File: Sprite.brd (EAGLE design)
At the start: 35 x 35 mm, 28 parts, among them P1 SPRITE_PIN, P2 SPRITE_PIN, U1 CC430F5137, U2 LSM9DS1, X1 TCXO_7Z

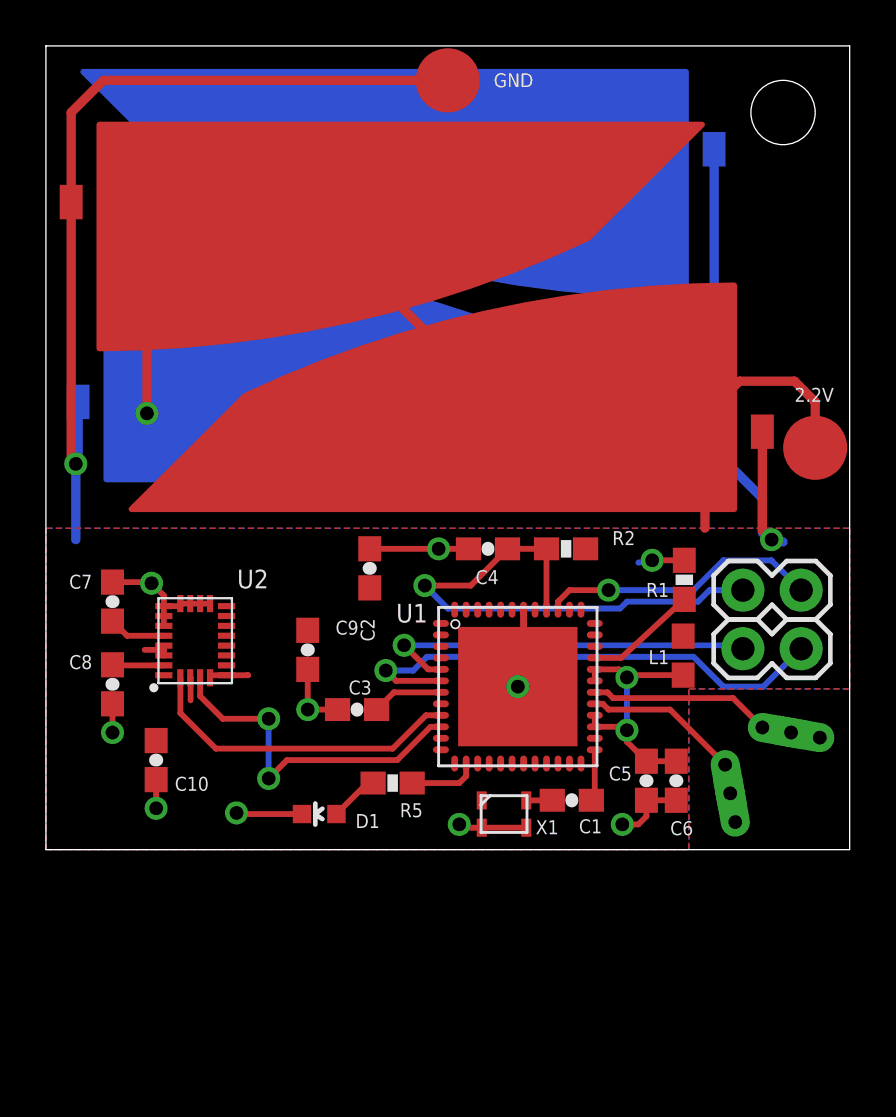
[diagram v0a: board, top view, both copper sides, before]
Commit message: New outline with board spring
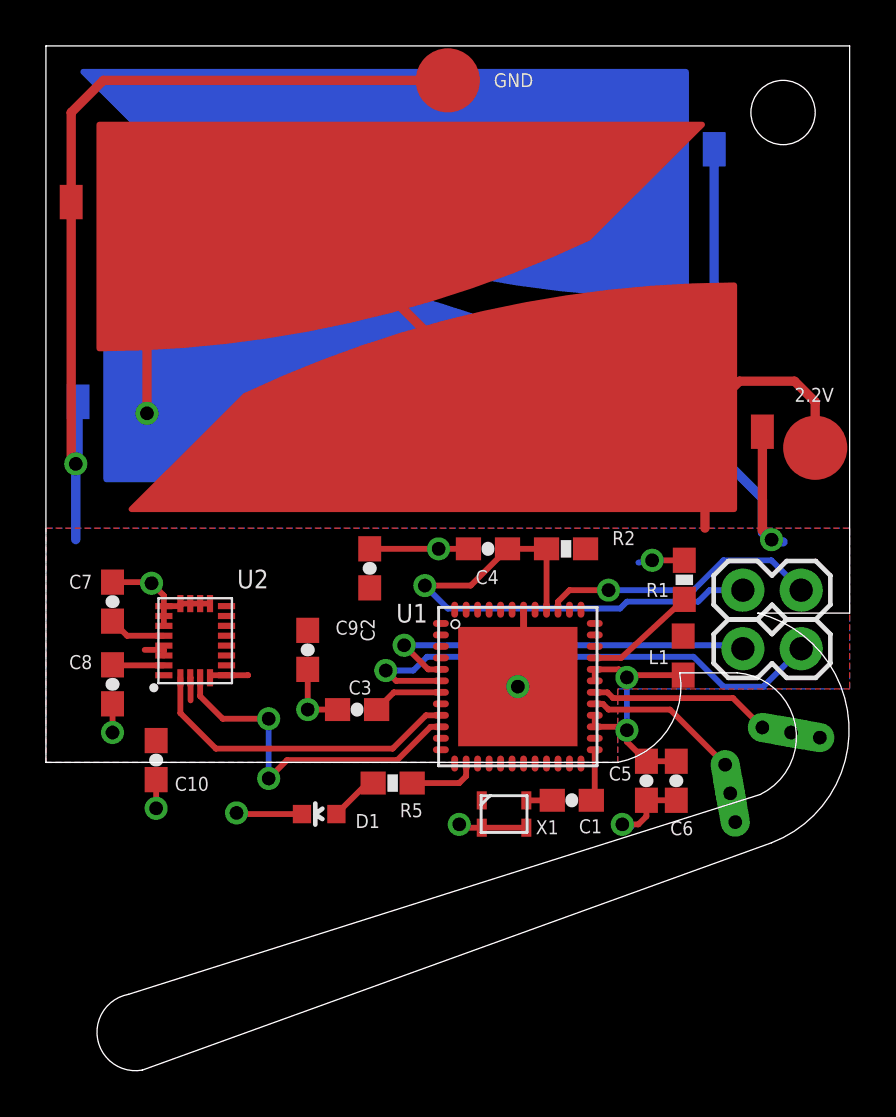
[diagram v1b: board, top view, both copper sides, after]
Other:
- board size 35 x 35 mm -> 35 x 44.6 mm

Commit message: moved solar cells + antenna on new board
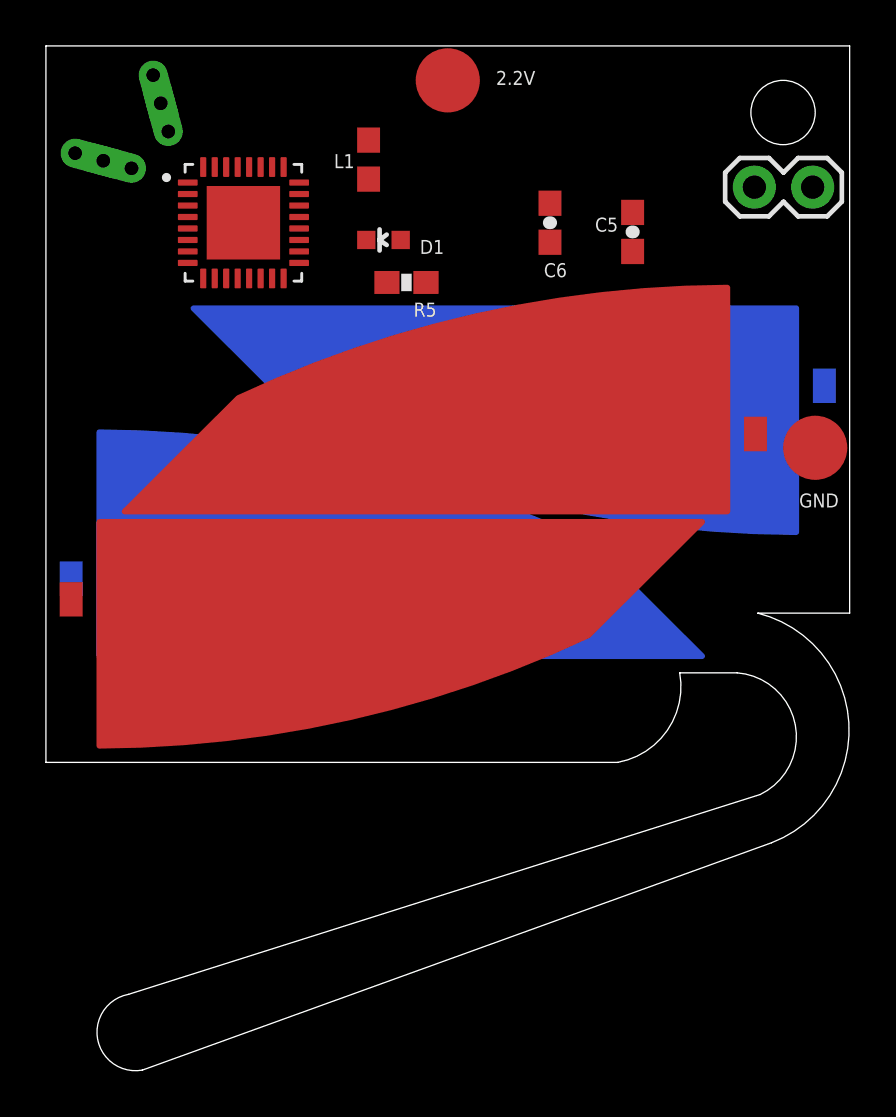
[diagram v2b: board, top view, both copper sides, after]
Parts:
- removed C1: 10 nF, SparkFun:0603-CAP
- removed C10: 10uF, SparkFun:0603-CAP
- removed C2, C3: 470nF, SparkFun:0603-CAP
- removed C4: 2.2nF, SparkFun:0603-CAP
- removed C7: 10nF, SparkFun:0603-CAP
- removed C8, C9: 0.1uF, SparkFun:0603-CAP
- removed JP2: (no value), SparkFun:1X02
- removed R1: 56K, SparkFun:0603-RES
- removed R2: 47K, SparkFun:0603-RES
- removed U2: LSM9DS1, LSM9DS1:LGA24-8X4
- removed X1: TCXO_7Z, SpriteTCXO:TXC_7Z
- U1: value CC430F5137 -> CC1310F128RHB; device TI_MSP430_v16:RGZ48 -> CC1310F128RHB:QFN50P500X500X100-33N
- moved ANT-P 39.0 mm to (5.00, 32.5), turned to 105 degrees
- moved ANT-N 38.9 mm to (2.50, 30.0), turned to 345 degrees
- moved S4 36.4 mm to (2.20, 8.30), turned to 0 degrees
- moved S2 32.5 mm to (29.8, 14.6), turned to 0 degrees
- moved S3 31.3 mm to (32.8, 23.7), turned to 180 degrees
- moved S1 27.9 mm to (2.20, 14.4), turned to 180 degrees
- moved L1 25.6 mm to (14.1, 30.1)
- moved D1 25.2 mm to (14.7, 26.6)
- moved C6 24.9 mm to (21.9, 27.3)
- moved C5 23.9 mm to (25.6, 26.9)
- moved U1 23.5 mm to (8.60, 27.3)
- moved R5 21.8 mm to (15.7, 24.7)
- moved JP3 20.1 mm to (30.9, 28.9)
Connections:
- removed net N$1: C1.1, U1.25
- removed net N$12: C1.2, X1.OUT
- removed net N$3: R1.1, U1.33
- removed net N$4: C3.1, U1.7
- removed net N$5: C7.1, U2.21
- removed net N$6: C8.1, U2.24
- removed net RST: C4.2, JP2.1, R2.1, U1.40
- removed net SCL: U1.9, U2.2
- removed net SDA: U1.10, U2.4
- removed net TEST: JP2.2, U1.39
- new net VDDR: U1.29
- new net VDDR_RF: U1.32
- new net VDDS: U1.28
- new net VDDSZ: U1.11
- new net VDDS_DCDC: U1.18
- net GND: now also P2.PIN; no longer C10.2, C2.2, C3.2, C4.1, C7.2, C8.2, C9.2, P1.PIN, R1.2, U1.42, U1.TP, U2.14, U2.15, U2.16, U2.17, U2.18, U2.19, U2.20, X1.GND1, X1.GND2
- net N$2: no longer U1.14
- net RFN: now also U1.2; no longer U1.30
- net RFP: now also U1.1; no longer U1.29
- net UART_RX: no longer U1.6
- net UART_TX: no longer U1.5
- net VCC: now also P1.PIN; no longer C10.1, C2.1, C9.1, P2.PIN, R2.2, U1.22, U1.34, U1.41, U1.45, U1.8, U2.1, U2.22, U2.23, U2.3, U2.5, U2.6, U2.7, U2.8, X1.VCC
- net VCCRF: no longer U1.27, U1.28, U1.31, U1.32
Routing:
- net GND: track 93.2 -> 0.00 mm, vias 12 -> 0
- net VCC: track 86.6 -> 0.00 mm, vias 1 -> 0
- net RST: track 23.2 -> 0.00 mm, vias 1 -> 0
- net UART_RX: track 22.1 -> 0.00 mm, vias 1 -> 0
- net UART_TX: track 16.8 -> 0.00 mm, vias 1 -> 0
- net SDA: track 15.2 -> 0.00 mm, vias 2 -> 0
- net SCL: track 14.1 -> 0.00 mm
- net TEST: track 12.2 -> 0.00 mm, vias 1 -> 0
- net VCCRF: track 11.8 -> 0.00 mm, vias 2 -> 0
- net RFN: track 11.7 -> 0.00 mm
- net RFP: track 10.6 -> 0.00 mm
- net N$3: track 4.90 -> 0.00 mm
- net N$4: track 3.11 -> 0.00 mm
- net N$2: track 3.02 -> 0.00 mm
- net N$5: track 2.50 -> 0.00 mm
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- removed copper zone on layer 16, net GND
- removed copper zone on layer 1, net VCC
